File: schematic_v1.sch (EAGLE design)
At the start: 0 parts

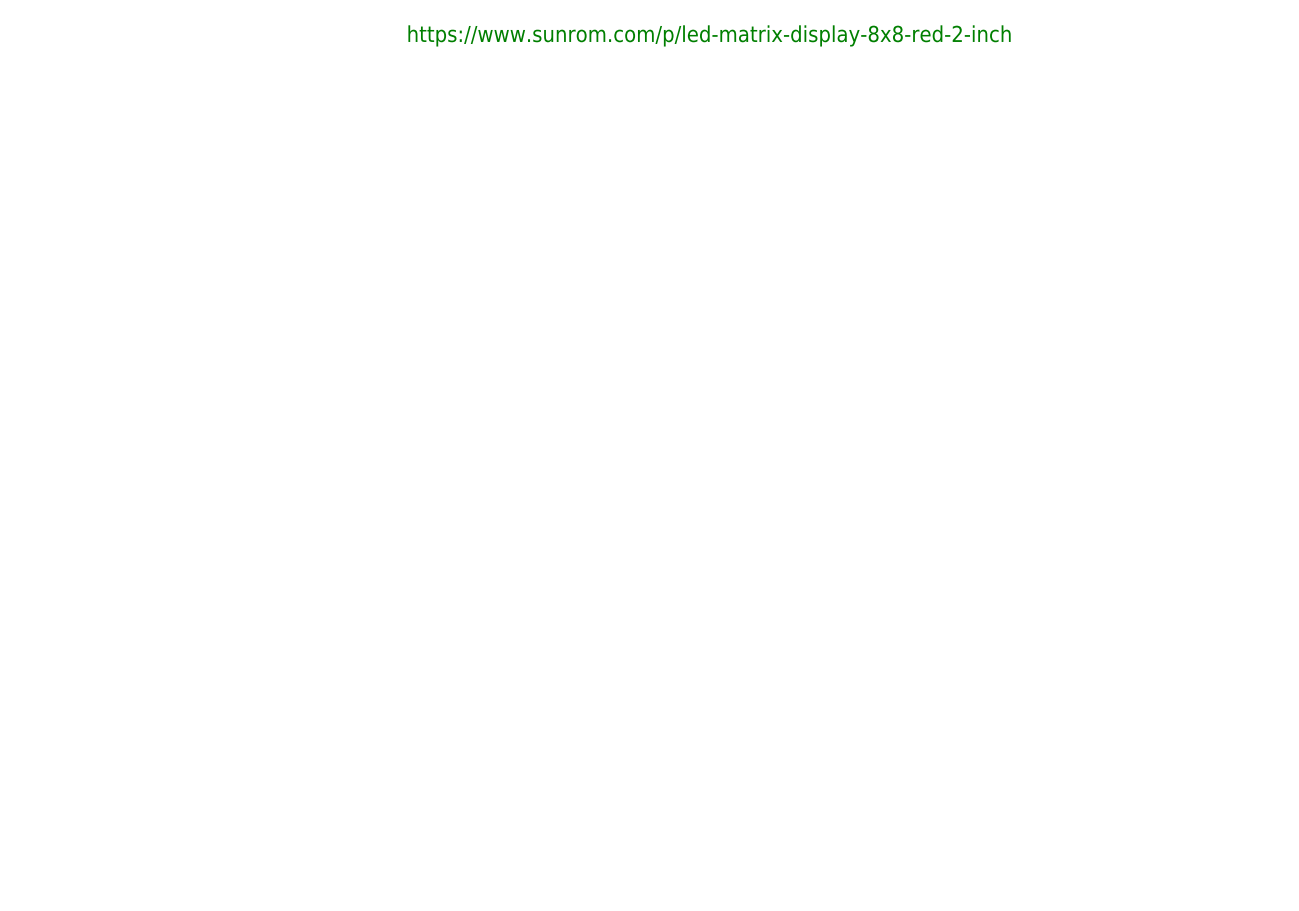
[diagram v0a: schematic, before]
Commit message: added max7219cwg library
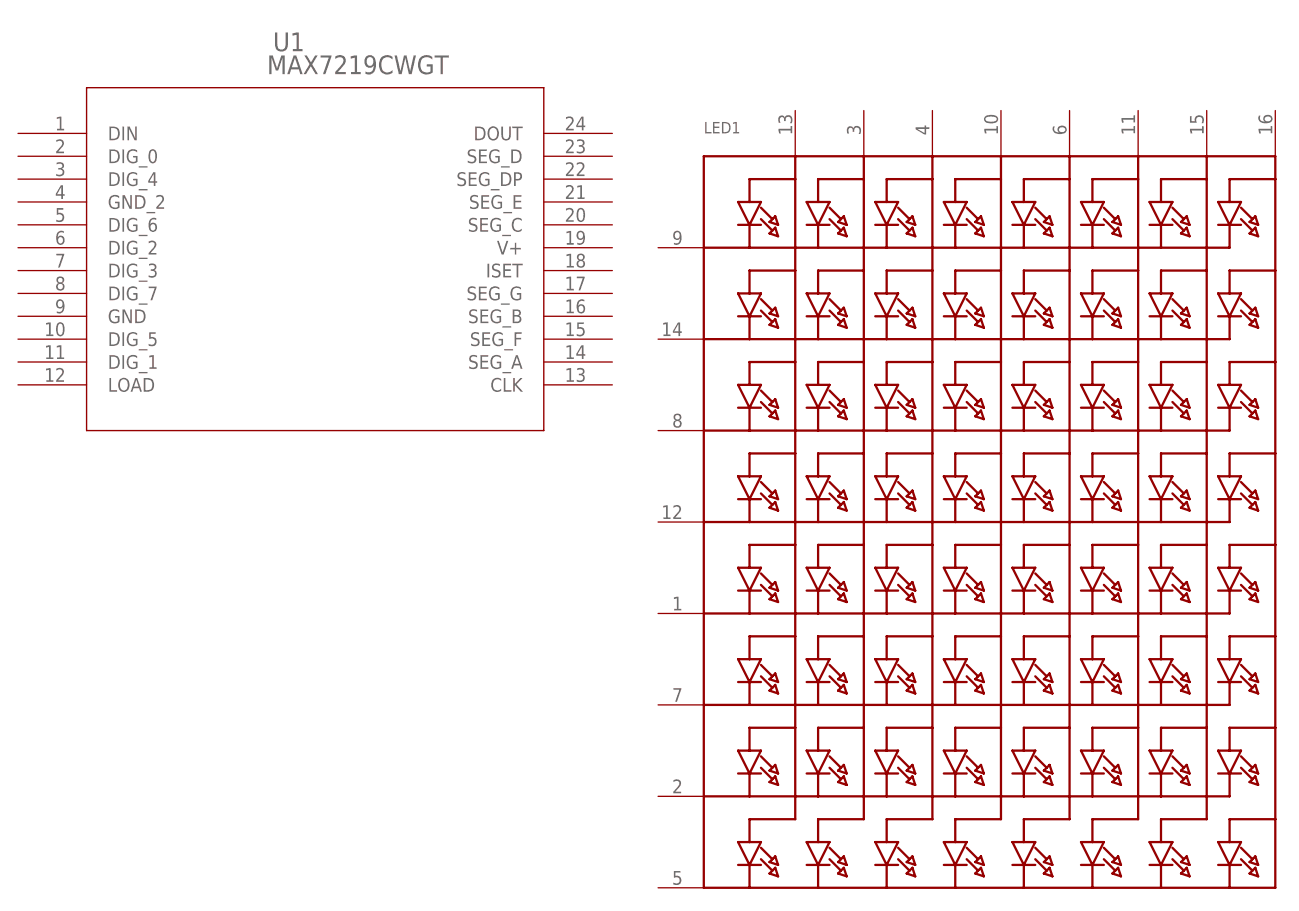
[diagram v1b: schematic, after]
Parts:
- added LED1: (no value), adafruit:SEGMENT_8X8_ROWCATHODEBL-M15
- added U1: MAX7219CWGT, MAX7219CWGT:MAX7219CWGT
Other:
- note removed: "https://www.sunrom.com/p/led-matrix-display-8x8-red-2-inch"

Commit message: Update schematic_v1.sch
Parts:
- added C1, C2, C3, C4: 10uF, SparkFun-Capacitors:10UF-0805-10V-10%
- added G1: BATTERY-HOLDER_11.6MM, battery:BATTERY-HOLDER_11.6MM
- added LED2: (no value), adafruit:SEGMENT_8X8_ROWCATHODEBL-M15
- added R1, R2: 103, adafruit:R-US_M0805
- added U2: MAX7219CWGT, MAX7219CWGT:MAX7219CWGT
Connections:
- new net CLK: U1.CLK, U2.CLK
- new net DIN: U1.DIN
- new net GND: C1.1, C2.1, C3.1, C4.1, G1.-, U1.GND, U1.GND_2, U2.GND, U2.GND_2
- new net LOAD: U1.LOAD, U2.LOAD
- new net N$10: LED1.A6, U1.DIG_5
- new net N$11: LED1.A2, U1.DIG_1
- new net N$12: LED2.A5, U2.DIG_4
- new net N$13: LED1.K1, U1.SEG_DP
- new net N$14: LED1.K2, U1.SEG_A
- new net N$15: LED1.K3, U1.SEG_B
- new net N$16: LED1.K4, U1.SEG_C
- new net N$17: LED1.K5, U1.SEG_D
- new net N$18: LED1.K6, U1.SEG_E
- new net N$19: LED1.K7, U1.SEG_F
- new net N$2: LED1.A1, U1.DIG_0
- new net N$20: LED1.K8, U1.SEG_G
- new net N$21: U1.DOUT, U2.DIN
- new net N$22: LED2.A7, U2.DIG_6
- new net N$23: R1.2, U1.ISET
- new net N$24: LED2.A3, U2.DIG_2
- new net N$25: LED2.A4, U2.DIG_3
- new net N$26: LED2.A8, U2.DIG_7
- new net N$27: LED2.A6, U2.DIG_5
- new net N$28: LED2.A2, U2.DIG_1
- new net N$29: LED2.K1, U2.SEG_DP
- new net N$3: LED1.A5, U1.DIG_4
- new net N$30: LED2.K2, U2.SEG_A
- new net N$31: LED2.K3, U2.SEG_B
- new net N$32: LED2.K4, U2.SEG_C
- new net N$33: LED2.K5, U2.SEG_D
- new net N$34: LED2.K6, U2.SEG_E
- new net N$35: LED2.K7, U2.SEG_F
- new net N$36: LED2.K8, U2.SEG_G
- new net N$37: U2.DOUT
- new net N$38: R2.2, U2.ISET
- new net N$5: LED1.A7, U1.DIG_6
- new net N$6: LED1.A3, U1.DIG_2
- new net N$7: LED1.A4, U1.DIG_3
- new net N$8: LED1.A8, U1.DIG_7
- new net N$9: LED2.A1, U2.DIG_0
- new net VCC: C1.2, C2.2, C3.2, C4.2, G1.+, R1.1, R2.1, U1.V+, U2.V+
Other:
- moved on the sheet: LED1, U1
